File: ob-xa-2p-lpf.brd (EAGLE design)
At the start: 104.1 x 79.7 mm, 35 parts, among them IC1 AS3320

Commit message: draft
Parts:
- removed R19: 10k, pot:B64Y
- removed R6: 500k, pot:B64Y
- added C10, C11, C12, C13: 100n, rcl:E1,8-4
- added C7, C9: 100n, rcl:C050-025X075
- added C8: 10u, rcl:E1,8-4
- added IC2: (no value), linear:TO220H
- added POWER_IN: (no value), pinhead:1X04
- added R22: 47, rcl:0207/10
- added RES_ADJ: 500k, pot:S63P
- added V/OCT_ADJ: 10k, pot:S63P
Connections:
- new net -15V: C12.-, POWER_IN.4, R22.2
- new net N$21: C7.2, C8.-, IC2.2, R22.1
- net +15V: now also C10.+, C13.+, POWER_IN.1
- net -5V: now also C11.-, C9.2, IC2.3
- net 0V: now also C10.-, C11.+, C12.+, C13.-, C7.1, C8.+, C9.1, IC2.1, POWER_IN.2, POWER_IN.3
- net FREQ_CV: now also V/OCT_ADJ.E, V/OCT_ADJ.S; no longer R19.S
- net N$15: now also RES_ADJ.E, RES_ADJ.S; no longer R6.S
- net N$2: now also V/OCT_ADJ.A; no longer R19.A
- net VIN: now also RES_ADJ.A; no longer R6.A

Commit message: add cv imput
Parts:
- added C14, C15: 0u1, rcl:C050-025X075
- added FREQ_CV_2: OFFBOARD2JACKALT, aarons_library:OFFBOARD2JACKALT
- added IC3: TL082P, linear:DIL08
- added R19, R23: 100k, rcl:0207/10
- added R24: 150k, rcl:0207/10
- added R25: 1M5, rcl:0207/10
- added R26, R27, R28: 100k, pot:B64Y
- added R6: 180k, rcl:0207/10
- C12, C13: value 100n -> 10u
- R20: value 44.2k -> 56k
- moved C10 85.8 mm to (62.2, 11.4)
- moved C11 83.1 mm to (54.6, 14.0)
- moved POWER_IN 60.1 mm to (3.81, 8.89), turned to 90 degrees
- moved IC2 58.7 mm to (12.7, -41.9), turned to 180 degrees
- moved C12 55.7 mm to (11.4, 11.4), turned to 90 degrees
- moved C13 54.5 mm to (11.4, 5.08), turned to 90 degrees
- moved C8 34.9 mm to (19.1, -21.6), turned to 90 degrees
- moved C7 33.1 mm to (15.2, -21.6), turned to 90 degrees
- moved R22 29.6 mm to (19.1, -11.4), turned to 90 degrees
- moved C9 22.9 mm to (10.2, -21.6), turned to 90 degrees
- renumbered FREQ_CV to FREQ_CV_1
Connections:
- removed net FREQ_CV: FREQ_CV_1.SIGNAL, V/OCT_ADJ.E, V/OCT_ADJ.S
- new net N$22: IC3.6, IC3.7
- new net N$23: IC3.2, R19.2, R23.2, R24.2, R25.2, R6.1, V/OCT_ADJ.A
- new net N$24: FREQ_CV_1.SIGNAL, R19.1
- new net N$25: R23.1, R26.S
- new net N$26: FREQ_CV_2.SIGNAL, R26.A
- new net N$27: R24.1, R28.S
- new net N$28: R25.1, R27.S
- new net V+: IC3.8
- new net V-: IC3.4
- net +15V: now also R27.A, R28.A
- net -15V: now also R6.2
- net 0V: now also C14.1, C15.2, FREQ_CV_2.GND, IC3.3, IC3.5, R26.E, R27.E, R28.E
- net N$2: now also IC3.1, V/OCT_ADJ.E, V/OCT_ADJ.S; no longer V/OCT_ADJ.A

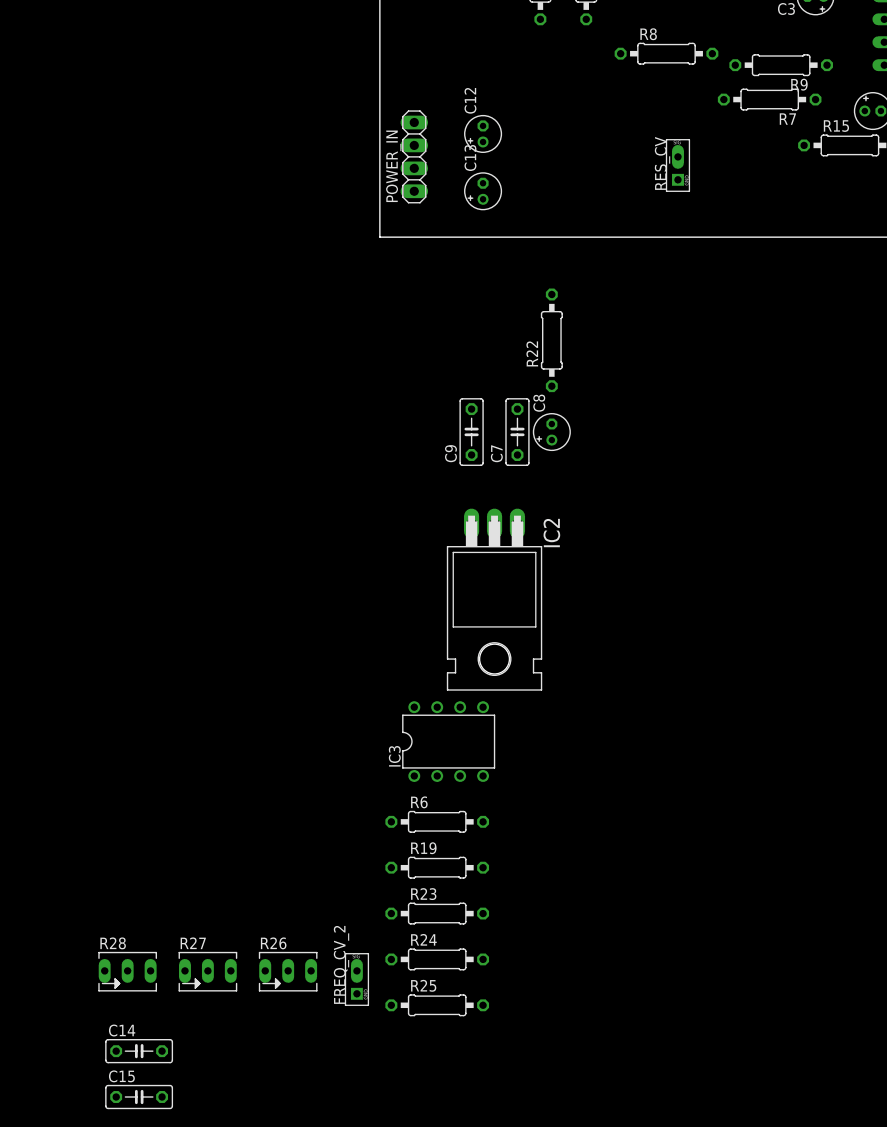
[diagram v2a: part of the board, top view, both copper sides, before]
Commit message: add res ctrl
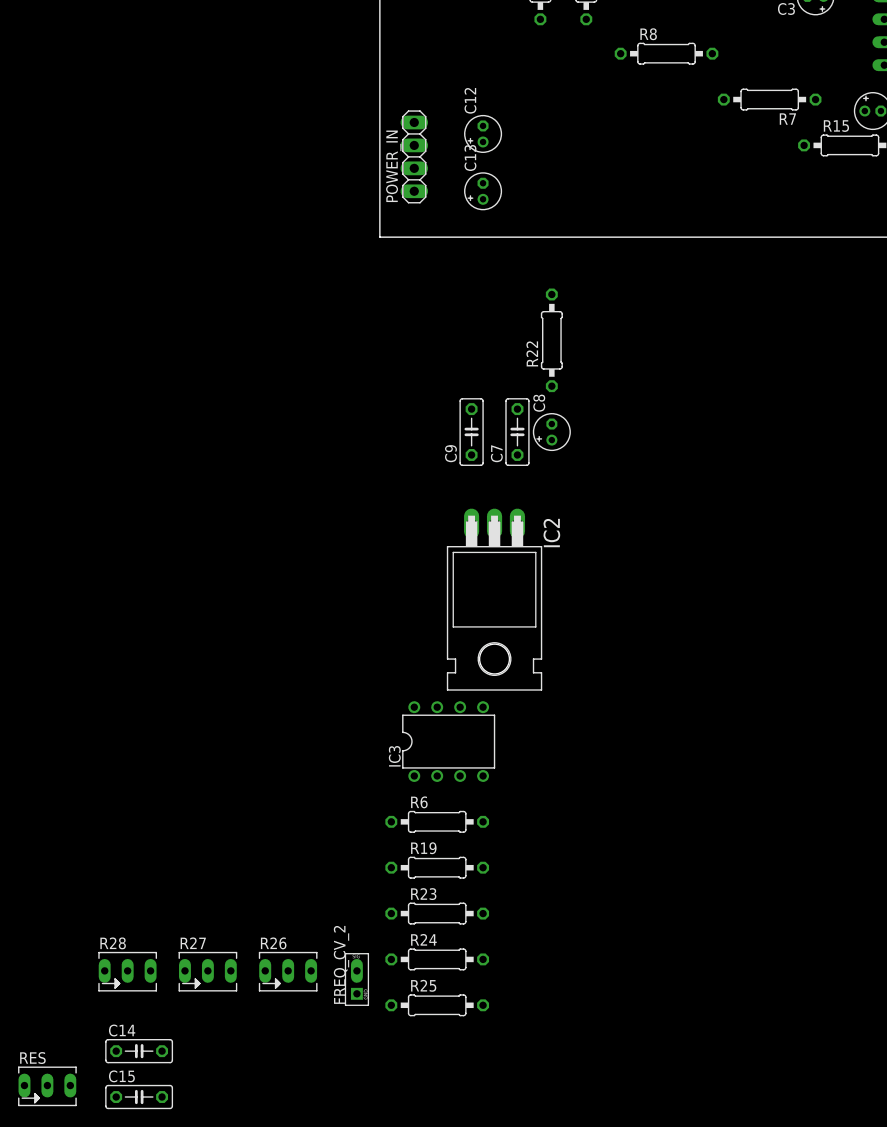
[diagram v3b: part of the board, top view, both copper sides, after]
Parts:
- removed R9: 330k, rcl:0207/10
- removed RES_CV: OFFBOARD2JACKALT, aarons_library:OFFBOARD2JACKALT
- added RES: 100k, pot:B64Y
- R7: value 33k -> 200k
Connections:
- net +15V: now also RES.E
- net -5V: no longer R9.2
- net 0V: now also RES.A; no longer RES_CV.GND
- net N$17: no longer R9.1
- net N$19: now also RES.S; no longer RES_CV.SIGNAL
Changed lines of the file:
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@@
 <attribute name="VALUE" x="57.15" y="45.085" size="1.27" layer="27" ratio="10" rot="R90"/>
 </element>
-<element name="R7" library="rcl" library_urn="urn:adsk.eagle:library:334" package="0207/10" package3d_urn="urn:adsk.eagle:package:23491/2" value="33k" x="43.18" y="15.24" smashed="yes" rot="R180">
+<element name="R7" library="rcl" library_urn="urn:adsk.eagle:library:334" package="0207/10" package3d_urn="urn:adsk.eagle:package:23491/2" value="200k" x="43.18" y="15.24" smashed="yes" rot="R180">
 <attribute name="NAME" x="46.228" y="13.716" size="1.27" layer="25" ratio="10" rot="R180"/>
 <attribute name="POPULARITY" value="36" x="11.43" y="50.8" size="1.778" layer="27" rot="R180" display="off"/>
@@
 <attribute name="VALUE" x="29.4894" y="19.685" size="1.27" layer="27" ratio="10"/>
 </element>
-<element name="R9" library="rcl" library_urn="urn:adsk.eagle:library:334" package="0207/10" package3d_urn="urn:adsk.eagle:package:23491/2" value="330k" x="44.45" y="19.05" smashed="yes" rot="R180">
-<attribute name="NAME" x="47.498" y="17.526" size="1.27" layer="25" ratio="10" rot="R180"/>
-<attribute name="POPULARITY" value="36" x="25.4" y="59.69" size="1.778" layer="27" rot="R180" display="off"/>
-<attribute name="SPICEPREFIX" value="R" x="25.4" y="59.69" size="1.778" layer="27" rot="R180" display="off"/>
-<attribute name="VALUE" x="46.7106" y="19.685" size="1.27" layer="27" ratio="10" rot="R180"/>
-</element>
-<element name="RES_CV" library="aarons_library" package="OFFBOARD2JACKALT" value="OFFBOARD2JACKALT" x="34.29" y="7.62" smashed="yes">
-<attribute name="NAME" x="31.75" y="5.08" size="1.27" layer="21" rot="R90"/>
-</element>
 <element name="IC2" library="linear" library_urn="urn:adsk.eagle:library:262" package="TO220H" package3d_urn="urn:adsk.eagle:package:16414/1" value="" x="12.7" y="-41.91" smashed="yes" rot="R180">
 <attribute name="NAME" x="18.161" y="-30.988" size="1.778" layer="25" ratio="10" rot="R270"/>
@@
 <attribute name="SPICEPREFIX" value="C" x="-26.67" y="-95.25" size="1.778" layer="27" display="off"/>
 <attribute name="VALUE" x="-30.099" y="-98.044" size="1.27" layer="27" ratio="10"/>
+</element>
+<element name="RES" library="pot" library_urn="urn:adsk.eagle:library:331" package="B64Y" package3d_urn="urn:adsk.eagle:package:22690/1" value="100k" x="-36.83" y="-93.98" smashed="yes">
+<attribute name="NAME" x="-40.005" y="-91.567" size="1.27" layer="25" ratio="10"/>
+<attribute name="POPULARITY" value="10" x="-36.83" y="-93.98" size="1.778" layer="27" display="off"/>
+<attribute name="VALUE" x="-40.005" y="-97.79" size="1.27" layer="27" ratio="10"/>
 </element>
 </elements>
@@
 <contactref element="D3" pad="C"/>
 <contactref element="AUDIO_OUT" pad="GND"/>
-<contactref element="RES_CV" pad="GND"/>
 <contactref element="C4" pad="2"/>
 <contactref element="C5" pad="2"/>
@@
 <contactref element="C15" pad="2"/>
 <contactref element="C14" pad="1"/>
+<contactref element="RES" pad="A"/>
 <wire x1="91.44" y1="43.18" x2="80.01" y2="58.42" width="0" layer="19" extent="1-1"/>
 <wire x1="86.36" y1="31.75" x2="91.44" y2="43.18" width="0" layer="19" extent="1-1"/>
@@
 <wire x1="44.45" y1="48.26" x2="45.72" y2="31.75" width="0" layer="19" extent="1-1"/>
 <wire x1="33.02" y1="54.61" x2="44.45" y2="48.26" width="0" layer="19" extent="1-1"/>
-<wire x1="33.02" y1="6.35" x2="53.721" y2="13.97" width="0" layer="19" extent="1-1"/>
-<wire x1="11.43" y1="5.969" x2="33.02" y2="6.35" width="0" layer="19" extent="1-1"/>
-<wire x1="11.43" y1="10.541" x2="11.43" y2="5.969" width="0" layer="19" extent="1-1"/>
+<wire x1="11.43" y1="10.541" x2="45.72" y2="31.75" width="0" layer="19" extent="1-1"/>
+<wire x1="11.43" y1="5.969" x2="11.43" y2="10.541" width="0" layer="19" extent="1-1"/>
 <wire x1="3.81" y1="10.16" x2="11.43" y2="10.541" width="0" layer="19" extent="1-1"/>
 <wire x1="3.81" y1="7.62" x2="3.81" y2="10.16" width="0" layer="19" extent="1-1"/>
@@
 <wire x1="-30.48" y1="-81.28" x2="-21.59" y2="-81.28" width="0" layer="19" extent="1-1"/>
 <wire x1="-29.21" y1="-90.17" x2="-30.48" y2="-81.28" width="0" layer="19" extent="1-1"/>
+<wire x1="-34.29" y1="-93.98" x2="-29.21" y2="-90.17" width="0" layer="19" extent="1-1"/>
 <wire x1="-24.13" y1="-95.25" x2="-29.21" y2="-90.17" width="0" layer="19" extent="1-1"/>
 </signal>
@@
 <contactref element="R28" pad="A"/>
 <contactref element="R27" pad="A"/>
-<wire x1="63.5" y1="29.21" x2="83.82" y2="36.83" width="0" layer="19" extent="1-1"/>
-<wire x1="61.341" y1="11.43" x2="63.5" y2="29.21" width="0" layer="19" extent="1-1"/>
-<wire x1="11.43" y1="4.191" x2="61.341" y2="11.43" width="0" layer="19" extent="1-1"/>
-<wire x1="3.81" y1="5.08" x2="11.43" y2="4.191" width="0" layer="19" extent="1-1"/>
-<wire x1="-16.51" y1="-81.28" x2="3.81" y2="5.08" width="0" layer="19" extent="1-1"/>
-<wire x1="-25.4" y1="-81.28" x2="-16.51" y2="-81.28" width="0" layer="19" extent="1-1"/>
+<contactref element="RES" pad="E"/>
+<wire x1="-25.4" y1="-81.28" x2="-39.37" y2="-93.98" width="0" layer="19" extent="1-1"/>
+<wire x1="-16.51" y1="-81.28" x2="-25.4" y2="-81.28" width="0" layer="19" extent="1-1"/>
+<wire x1="3.81" y1="5.08" x2="-16.51" y2="-81.28" width="0" layer="19" extent="1-1"/>
+<wire x1="11.43" y1="4.191" x2="3.81" y2="5.08" width="0" layer="19" extent="1-1"/>
+<wire x1="61.341" y1="11.43" x2="11.43" y2="4.191" width="0" layer="19" extent="1-1"/>
+<wire x1="63.5" y1="29.21" x2="61.341" y2="11.43" width="0" layer="19" extent="1-1"/>
+<wire x1="83.82" y1="36.83" x2="63.5" y2="29.21" width="0" layer="19" extent="1-1"/>
 </signal>
 <signal name="N$10">
@@
 <signal name="-5V">
 <contactref element="R15" pad="1"/>
-<contactref element="R9" pad="2"/>
 <contactref element="IC2" pad="3"/>
 <contactref element="C9" pad="2"/>
 <contactref element="C11" pad="-"/>
 <wire x1="46.99" y1="10.16" x2="55.499" y2="13.97" width="0" layer="19" extent="1-1"/>
-<wire x1="39.37" y1="19.05" x2="46.99" y2="10.16" width="0" layer="19" extent="1-1"/>
 <wire x1="10.16" y1="-19.05" x2="46.99" y2="10.16" width="0" layer="19" extent="1-1"/>
 <wire x1="10.16" y1="-31.75" x2="10.16" y2="-19.05" width="0" layer="19" extent="1-1"/>
@@
 </signal>
 <signal name="N$17">
+<contactref element="IC1" pad="9"/>
 <contactref element="R7" pad="1"/>
-<contactref element="R9" pad="1"/>
-<contactref element="IC1" pad="9"/>
-<wire x1="49.53" y1="19.05" x2="55.88" y2="19.05" width="0" layer="19" extent="1-1"/>
-<wire x1="48.26" y1="15.24" x2="49.53" y2="19.05" width="0" layer="19" extent="1-1"/>
-</signal>
-<signal name="N$19">
-<contactref element="R7" pad="2"/>
-<contactref element="RES_CV" pad="SIGNAL"/>
-<wire x1="33.02" y1="8.89" x2="38.1" y2="15.24" width="0" layer="19" extent="1-1"/>
+<wire x1="48.26" y1="15.24" x2="55.88" y2="19.05" width="0" layer="19" extent="1-1"/>
 </signal>
 <signal name="N$18">
@@
 <contactref element="IC3" pad="8"/>
 </signal>
+<signal name="N$19">
+<contactref element="RES" pad="S"/>
+<contactref element="R7" pad="2"/>
+<wire x1="38.1" y1="15.24" x2="-36.83" y2="-93.98" width="0" layer="19" extent="1-1"/>
+</signal>
 </signals>

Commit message: drop -5V
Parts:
- R15: value 270 -> 1K5
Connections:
- net -15V: now also C11.-, R15.1
- net -5V: no longer C11.-, R15.1
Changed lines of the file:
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@@
 <attribute name="VALUE" x="73.025" y="34.0106" size="1.27" layer="27" ratio="10" rot="R270"/>
 </element>
-<element name="R15" library="rcl" library_urn="urn:adsk.eagle:library:334" package="0207/10" package3d_urn="urn:adsk.eagle:package:23491/2" value="270" x="52.07" y="10.16" smashed="yes">
+<element name="R15" library="rcl" library_urn="urn:adsk.eagle:library:334" package="0207/10" package3d_urn="urn:adsk.eagle:package:23491/2" value="1K5" x="52.07" y="10.16" smashed="yes">
 <attribute name="NAME" x="49.022" y="11.684" size="1.27" layer="25" ratio="10"/>
 <attribute name="POPULARITY" value="36" x="71.12" y="-40.64" size="1.778" layer="27" display="off"/>
@@
 </signal>
 <signal name="-5V">
-<contactref element="R15" pad="1"/>
 <contactref element="IC2" pad="3"/>
 <contactref element="C9" pad="2"/>
-<contactref element="C11" pad="-"/>
-<wire x1="46.99" y1="10.16" x2="55.499" y2="13.97" width="0" layer="19" extent="1-1"/>
-<wire x1="10.16" y1="-19.05" x2="46.99" y2="10.16" width="0" layer="19" extent="1-1"/>
-<wire x1="10.16" y1="-31.75" x2="10.16" y2="-19.05" width="0" layer="19" extent="1-1"/>
+<wire x1="10.16" y1="-19.05" x2="10.16" y2="-31.75" width="0" layer="19" extent="1-1"/>
 </signal>
 <signal name="N$16">
@@
 <contactref element="C12" pad="-"/>
 <contactref element="R6" pad="2"/>
-<wire x1="19.05" y1="-6.35" x2="11.43" y2="-64.77" width="0" layer="19" extent="1-1"/>
+<contactref element="R15" pad="1"/>
+<contactref element="C11" pad="-"/>
+<wire x1="46.99" y1="10.16" x2="55.499" y2="13.97" width="0" layer="19" extent="1-1"/>
+<wire x1="19.05" y1="-6.35" x2="46.99" y2="10.16" width="0" layer="19" extent="1-1"/>
 <wire x1="11.43" y1="12.319" x2="19.05" y2="-6.35" width="0" layer="19" extent="1-1"/>
 <wire x1="3.81" y1="12.7" x2="11.43" y2="12.319" width="0" layer="19" extent="1-1"/>
+<wire x1="11.43" y1="-64.77" x2="19.05" y2="-6.35" width="0" layer="19" extent="1-1"/>
 </signal>
 <signal name="N$2">

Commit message: improve power
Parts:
- removed C7, C9: 100n, rcl:C050-025X075
- removed C8: 10u, rcl:E1,8-4
- removed IC2: (no value), linear:TO220H
- removed R22: 47, rcl:0207/10
- added L1, L2: (no value), rcl:0207/10
- renumbered R26 to CV2
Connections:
- removed net -5V: C9.2, IC2.3
- removed net N$21: C7.2, C8.-, IC2.2, R22.1
- removed net V+: IC3.8
- removed net V-: IC3.4
- new net N$29: L1.1, POWER_IN.1
- new net N$31: L2.1, POWER_IN.4
- net +15V: now also C15.1, IC3.8, L1.2; no longer POWER_IN.1
- net -15V: now also C14.2, IC3.4, L2.2; no longer POWER_IN.4, R22.2
- net 0V: no longer C7.1, C8.+, C9.1, IC2.1

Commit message: layout CV
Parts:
- removed R27, R28: 100k, pot:B64Y
- added COARSE, FINE: 100k, pot:B64Y
- moved CV2 177.9 mm to (135.9, 20.3), turned to 90 degrees
- moved FREQ_CV_2 176.1 mm to (135.9, 27.9), turned to 90 degrees
- moved R23 153.7 mm to (127.0, 20.3), turned to 180 degrees
- moved R24 152.2 mm to (127.0, 12.7), turned to 180 degrees
- moved R19 151.4 mm to (121.9, 27.9), turned to 270 degrees
- moved R25 150.6 mm to (127.0, 5.08), turned to 180 degrees
- moved IC3 128.6 mm to (115.6, 14.0), turned to 270 degrees
- moved R6 128.6 mm to (114.3, 5.08), turned to 180 degrees
- moved RES 126.2 mm to (38.1, 7.62)
- moved L1 124.3 mm to (11.4, 12.7)
- moved L2 121.9 mm to (11.4, 5.08)
- moved C14 101.9 mm to (33.0, -7.62)
- moved C15 100.8 mm to (33.0, -14.0)
- moved FREQ_CV_1 59.7 mm to (135.9, 33.0), turned to 90 degrees
- moved R21 35.9 mm to (104.1, 15.2), turned to 180 degrees
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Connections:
- net N$29 renamed +15V_IN
- net N$31 renamed -15V_IN
- net +15V: now also COARSE.A, FINE.A; no longer R27.A, R28.A
- net 0V: now also COARSE.E, FINE.E; no longer R27.E, R28.E
- net N$27: now also COARSE.S; no longer R28.S
- net N$28: now also FINE.S; no longer R27.S
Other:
- board size 104.1 x 79.7 mm -> 162.5 x 79.7 mm

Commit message: layout everything
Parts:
- moved FREQ_CV_1 88.4 mm to (47.5, 35.6)
- moved FREQ_CV_2 88.4 mm to (47.5, 30.5)
- moved V/OCT_ADJ 88.1 mm to (27.4, 25.7), turned to 0 degrees
- moved IC3 88.1 mm to (27.4, 14.5)
- moved R24 87.9 mm to (39.1, 10.7)
- moved R25 87.9 mm to (39.1, 6.35)
- moved COARSE 87.9 mm to (48.0, 14.0)
- moved CV2 87.9 mm to (48.0, 21.6)
- moved FINE 87.9 mm to (48.0, 6.35)
- moved R23 87.9 mm to (39.1, 21.1)
- moved R21 87.3 mm to (17.0, 20.3), turned to 90 degrees
- moved R6 86.9 mm to (27.4, 6.35)
- moved R20 84.1 mm to (20.1, 20.3), turned to 270 degrees
- moved R19 82.9 mm to (39.1, 24.4), turned to 180 degrees
- moved R16 68.4 mm to (23.1, 64.8), turned to 180 degrees
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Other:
- board size 162.5 x 79.7 mm -> 50.8 x 85.5 mm
